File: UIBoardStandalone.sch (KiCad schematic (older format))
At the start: 45 parts, among them J10 Conn_02x15_Odd_Even, J17 Conn_02x08_Odd_Even, SW1 Button_P, SW10 Button_4, SW11 Button_8, SW12 Button_0, SW13 Button_2, SW14 Button_5, SW15 Button_3, SW16 Button_6, SW17 Button_9, SW18 Button_Z, SW2 Button_X, SW3 Button_S, SW4 Button_G, SW5 Button_R, SW6 Button_M, SW7 Button_7, SW8 Button_Y, SW9 Button_1, U1 HD1077R, U10 MM74C923, U11 HD1077R, U12 HD1077R, U13 HD1077R, U14 HD1077R, U15 HD1077R, U16 HD1077R, U17 HD1077R, U2 HD1077R, U3 HD1077R, U4 HD1077R, U5 HD1077R, U6 HD1077R, U7 HD1077R, U8 HD1077R, U9 HD1077R

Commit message: - Outline und erste Plazierungen
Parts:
- added H1, H2, H3, H4, H5, H6: MountingHole, MountingHole:MountingHole_3.2mm_M3_DIN965, symbol Mechanical:MountingHole
- SW1: renamed from SW2; footprint (none) -> Button_Switch_SMD:SW_SPST_EVQP0
- SW10: renamed from SW16; footprint (none) -> Button_Switch_SMD:SW_SPST_EVQP0
- SW11: renamed from SW3; footprint (none) -> Button_Switch_SMD:SW_SPST_EVQP0
- SW12: renamed from SW7; footprint (none) -> Button_Switch_SMD:SW_SPST_EVQP0
- SW13: renamed from SW11; footprint (none) -> Button_Switch_SMD:SW_SPST_EVQP0
- SW14: renamed from SW17; footprint (none) -> Button_Switch_SMD:SW_SPST_EVQP0
- SW15: renamed from SW4; footprint (none) -> Button_Switch_SMD:SW_SPST_EVQP0
- SW16: renamed from SW8; footprint (none) -> Button_Switch_SMD:SW_SPST_EVQP0
- SW17: renamed from SW12; footprint (none) -> Button_Switch_SMD:SW_SPST_EVQP0
- SW18: footprint (none) -> Button_Switch_SMD:SW_SPST_EVQP0
- SW2: renamed from SW5; footprint (none) -> Button_Switch_SMD:SW_SPST_EVQP0
- SW3: renamed from SW9; footprint (none) -> Button_Switch_SMD:SW_SPST_EVQP0
- SW4: renamed from SW13; footprint (none) -> Button_Switch_SMD:SW_SPST_EVQP0
- SW5: renamed from SW15; footprint (none) -> Button_Switch_SMD:SW_SPST_EVQP0
- SW6: renamed from SW1; footprint (none) -> Button_Switch_SMD:SW_SPST_EVQP0
- SW7: renamed from SW6; footprint (none) -> Button_Switch_SMD:SW_SPST_EVQP0
- SW8: renamed from SW10; footprint (none) -> Button_Switch_SMD:SW_SPST_EVQP0
- SW9: renamed from SW14; footprint (none) -> Button_Switch_SMD:SW_SPST_EVQP0
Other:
- moved on the sheet: SW12, SW13, SW16, SW17

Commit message: - Outline / Postionierung Zwischenstand
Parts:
- renumbered C85 to C2, C86 to C3, J17 to J1, J10 to J2, R61 to R1, U11 to U10, U12 to U11, U13 to U12, U14 to U13, U15 to U14, U16 to U15, U17 to U16, U10 to U17
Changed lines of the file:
@@
 $EndDescr
 $Comp
-L Connector_Generic:Conn_02x08_Odd_Even J17
+L Connector_Generic:Conn_02x08_Odd_Even J1
 U 1 1 5F670C41
 P 14100 4400
-AR Path="/5F670C41" Ref="J17"  Part="1"
+AR Path="/5F670C41" Ref="J1"  Part="1"
 AR Path="/602283F4/5F670C41" Ref="J?"  Part="1"
 AR Path="/6101166B/5F670C41" Ref="J17"  Part="1"
-F 0 "J17" H 14150 4917 50  0000 C CNN
+F 0 "J1" H 14150 4917 50  0000 C CNN
 F 1 "Conn_02x08_Odd_Even" H 14150 4826 50  0000 C CNN
 F 2 "Connector_PinHeader_2.54mm:PinHeader_2x08_P2.54mm_Vertical" H 14100 4400 50  0001 C CNN
@@
 ButtonA2GND
 $Comp
-L 74xx:MM74C923 U10
+L 74xx:MM74C923 U17
 U 1 1 60D1026E
 P 12800 7000
-F 0 "U10" H 12950 7800 50  0000 C CNN
+F 0 "U17" H 12950 7800 50  0000 C CNN
 F 1 "MM74C923" H 13100 7700 50  0000 C CNN
 F 2 "Package_SO:SOIC-20W_7.5x12.8mm_P1.27mm" H 12800 7000 50  0001 C CNN
@@
 	13750 7200 13300 7200
 $Comp
-L Device:C C86
+L Device:C C3
 U 1 1 60DD134B
 P 14000 7650
-F 0 "C86" H 14115 7696 50  0000 L CNN
+F 0 "C3" H 14115 7696 50  0000 L CNN
 F 1 "224nF" H 14115 7605 50  0000 L CNN
 F 2 "" H 14038 7500 50  0001 C CNN
@@
 	14000 7400 14000 7500
 $Comp
-L Device:C C85
+L Device:C C2
 U 1 1 60E085DC
 P 13450 7650
-F 0 "C85" H 13565 7696 50  0000 L CNN
+F 0 "C2" H 13565 7696 50  0000 L CNN
 F 1 "52uF" H 13565 7605 50  0000 L CNN
 F 2 "" H 13488 7500 50  0001 C CNN
@@
 	8350 5250 10150 5250
 $Comp
-L Device:R_PHOTO R61
+L Device:R_PHOTO R1
 U 1 1 5FC1430B
 P 10800 4700
-F 0 "R61" H 10870 4746 50  0000 L CNN
+F 0 "R1" H 10870 4746 50  0000 L CNN
 F 1 "LDR" H 10870 4655 50  0000 L CNN
 F 2 "OptoDevice:R_LDR_4.9x4.2mm_P2.54mm_Vertical" V 10850 4450 50  0001 L CNN
@@
 	5050 7600 5050 7850
 $Comp
-L Connector_Generic:Conn_02x15_Odd_Even J10
+L Connector_Generic:Conn_02x15_Odd_Even J2
 U 1 1 60B2D605
 P 5550 4550
-AR Path="/60B2D605" Ref="J10"  Part="1"
+AR Path="/60B2D605" Ref="J2"  Part="1"
 AR Path="/6101166B/60B2D605" Ref="J10"  Part="1"
-F 0 "J10" H 5600 5467 50  0000 C CNN
+F 0 "J2" H 5600 5467 50  0000 C CNN
 F 1 "Conn_02x15_Odd_Even" H 5600 5376 50  0000 C CNN
 F 2 "Connector_PinHeader_2.54mm:PinHeader_2x15_P2.54mm_Vertical" H 5550 4550 50  0001 C CNN
@@
 $EndComp
 $Comp
-L TeKaDe:HD1077R U11
+L TeKaDe:HD1077R U10
 U 1 1 61191E3C
 P 9800 800
-F 0 "U11" H 9750 700 50  0000 L CNN
+F 0 "U10" H 9750 700 50  0000 L CNN
 F 1 "HD1077R" H 9600 800 50  0000 L CNN
 F 2 "TeKaDe:7SegmentLED_HD1077R" H 9800 900 50  0001 C CNN
@@
 $EndComp
 $Comp
-L TeKaDe:HD1077R U12
+L TeKaDe:HD1077R U11
 U 1 1 6119245E
 P 10500 800
-F 0 "U12" H 10450 700 50  0000 L CNN
+F 0 "U11" H 10450 700 50  0000 L CNN
 F 1 "HD1077R" H 10300 800 50  0000 L CNN
 F 2 "TeKaDe:7SegmentLED_HD1077R" H 10500 900 50  0001 C CNN
@@
 $EndComp
 $Comp
-L TeKaDe:HD1077R U13
+L TeKaDe:HD1077R U12
 U 1 1 61192B19
 P 11250 800
-F 0 "U13" H 11200 700 50  0000 L CNN
+F 0 "U12" H 11200 700 50  0000 L CNN
 F 1 "HD1077R" H 11050 800 50  0000 L CNN
 F 2 "TeKaDe:7SegmentLED_HD1077R" H 11250 900 50  0001 C CNN
@@
 $EndComp
 $Comp
-L TeKaDe:HD1077R U14
+L TeKaDe:HD1077R U13
 U 1 1 61193991
 P 12000 800
-F 0 "U14" H 11950 700 50  0000 L CNN
+F 0 "U13" H 11950 700 50  0000 L CNN
 F 1 "HD1077R" H 11800 800 50  0000 L CNN
 F 2 "TeKaDe:7SegmentLED_HD1077R" H 12000 900 50  0001 C CNN
@@
 $EndComp
 $Comp
-L TeKaDe:HD1077R U15
+L TeKaDe:HD1077R U14
 U 1 1 61194425
 P 12750 800
-F 0 "U15" H 12700 700 50  0000 L CNN
+F 0 "U14" H 12700 700 50  0000 L CNN
 F 1 "HD1077R" H 12550 800 50  0000 L CNN
 F 2 "TeKaDe:7SegmentLED_HD1077R" H 12750 900 50  0001 C CNN
@@
 $EndComp
 $Comp
-L TeKaDe:HD1077R U16
+L TeKaDe:HD1077R U15
 U 1 1 611949C1
 P 13450 800
-F 0 "U16" H 13400 700 50  0000 L CNN
+F 0 "U15" H 13400 700 50  0000 L CNN
 F 1 "HD1077R" H 13250 800 50  0000 L CNN
 F 2 "TeKaDe:7SegmentLED_HD1077R" H 13450 900 50  0001 C CNN
@@
 $EndComp
 $Comp
-L TeKaDe:HD1077R U17
+L TeKaDe:HD1077R U16
 U 1 1 6119568C
 P 14200 800
-F 0 "U17" H 14150 700 50  0000 L CNN
+F 0 "U16" H 14150 700 50  0000 L CNN
 F 1 "HD1077R" H 14000 800 50  0000 L CNN
 F 2 "TeKaDe:7SegmentLED_HD1077R" H 14200 900 50  0001 C CNN

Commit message: - erster Stand für Abmessungen
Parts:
- D1: value LED_RED -> LED_RD
- D2: value LED_YELLOW -> LED_YL
- D3: value LED_GREEN -> LED_GN
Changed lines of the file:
@@
 P 9650 4650
 F 0 "D1" V 9597 4730 50  0000 L CNN
-F 1 "LED_RED" V 9688 4730 50  0000 L CNN
+F 1 "LED_RD" V 9688 4730 50  0000 L CNN
 F 2 "LED_THT:LED_D5.0mm" H 9650 4650 50  0001 C CNN
 F 3 "~" H 9650 4650 50  0001 C CNN
@@
 P 9150 4650
 F 0 "D2" V 9097 4730 50  0000 L CNN
-F 1 "LED_YELLOW" V 9188 4730 50  0000 L CNN
+F 1 "LED_YL" V 9188 4730 50  0000 L CNN
 F 2 "LED_THT:LED_D5.0mm" H 9150 4650 50  0001 C CNN
 F 3 "~" H 9150 4650 50  0001 C CNN
@@
 P 8500 4650
 F 0 "D3" V 8447 4730 50  0000 L CNN
-F 1 "LED_GREEN" V 8538 4730 50  0000 L CNN
+F 1 "LED_GN" V 8538 4730 50  0000 L CNN
 F 2 "LED_THT:LED_D5.0mm" H 8500 4650 50  0001 C CNN
 F 3 "~" H 8500 4650 50  0001 C CNN

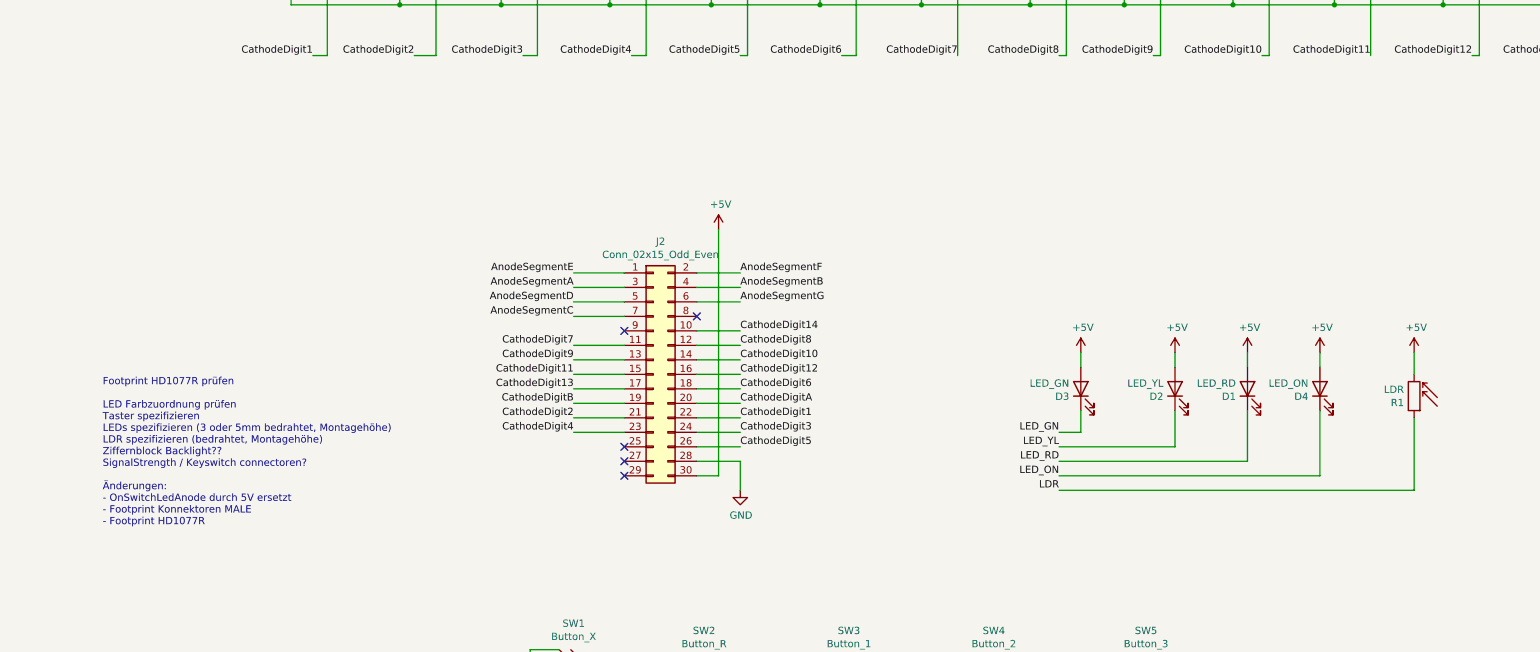
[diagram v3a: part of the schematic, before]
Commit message: [fix:] measurement errors [add:] backlight LEDs
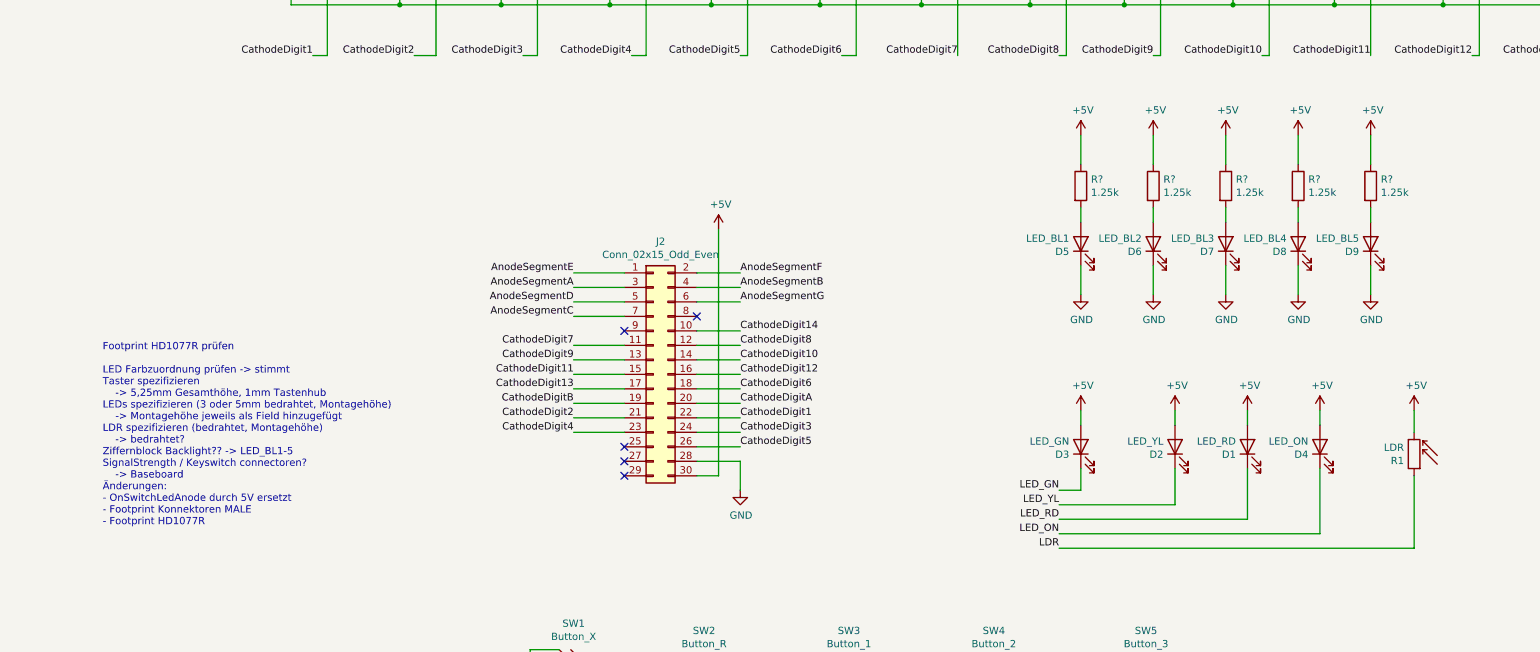
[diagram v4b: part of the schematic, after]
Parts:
- added D5: LED_BL1, LED_THT:LED_D3.0mm, symbol Device:LED
- added D6: LED_BL2, LED_THT:LED_D3.0mm, symbol Device:LED
- added D7: LED_BL3, LED_THT:LED_D3.0mm, symbol Device:LED
- added D8: LED_BL4, LED_THT:LED_D3.0mm, symbol Device:LED
- added D9: LED_BL5, LED_THT:LED_D3.0mm, symbol Device:LED
- added R? (x5): 1.25k, symbol Device:R
- D1, D2, D3: Montagehöhe (none) -> 9mm
- D4: Montagehöhe (none) -> 8mm
- R1: Montagehöhe (none) -> 7mm
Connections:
- net +5V: now also R?.1, R?.1, R?.1, R?.1, R?.1
- net GND: now also D5.1 (K), D6.1 (K), D7.1 (K), D8.1 (K), D9.1 (K)
- new net: D5.2 (A), R?.2
- new net: D6.2 (A), R?.2
- new net: D7.2 (A), R?.2
- new net: D8.2 (A), R?.2
- new net: D9.2 (A), R?.2
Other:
- note added: "Footprint HD1077R prüfen\n\nLED Farbzuordnung prüfen -> stimmt\nTaster spezifizieren\n -> 5,25mm Gesamthöhe, 1mm Tastenhub\nLEDs spezifizieren (3 oder 5mm bedrahtet, Montagehöhe)\n -> Montagehöhe jeweils als Field hinzugefügt\nLDR spezifizieren (bedrahtet, Montagehöhe)\n -> bedrahtet?\nZiffernblock Backlight?? -> LED_BL1-5\nSignalStrength / Keyswitch connectoren?\n -> Baseboard\nÄnderungen:\n- On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"
- note removed: "Footprint HD1077R prüfen\n\nLED Farbzuordnung prüfen\nTaster spezifizieren\nLEDs spezifizieren (3 oder 5mm bedrahtet, Montagehöhe)\nLDR spezifizieren (bedrahtet, Montagehöhe)\nZiffernblock Backlight??\nSignalStrength / Keyswitch connectoren?\n\nÄnderungen:\n- OnSwitchLedAnode durch 5V ersetzt\n- Footprint Konnektoren MALE\n- Footprint HD1077R"
- moved on the sheet: D1, D2, D3, D4, R1

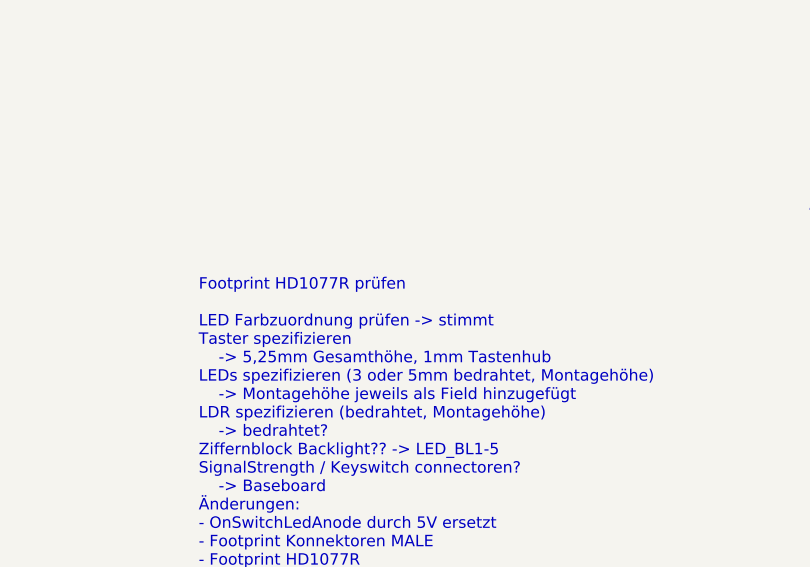
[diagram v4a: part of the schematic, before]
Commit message: [mod:] Note updates, KeySwitch mechanical definition
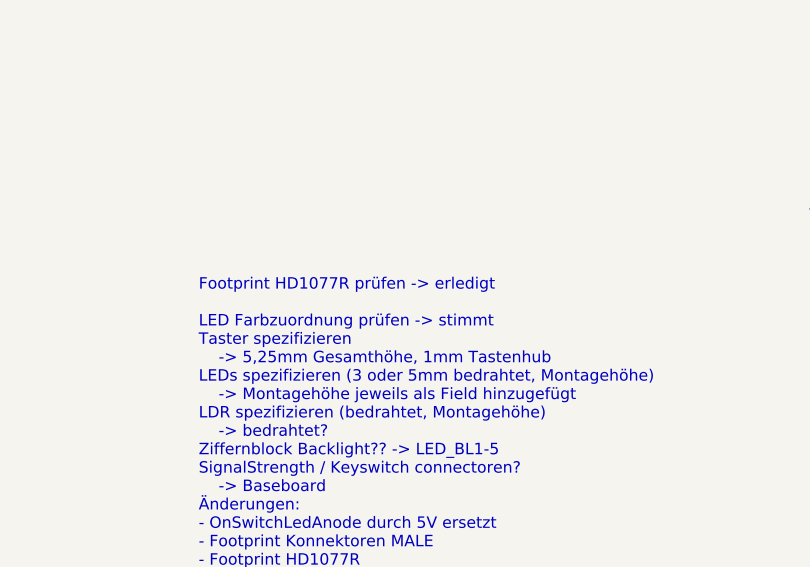
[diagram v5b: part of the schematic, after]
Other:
- note added: "Footprint HD1077R prüfen -> erledigt\n\nLED Farbzuordnung prüfen -> stimmt\nTaster spezifizieren\n -> 5,25mm Gesamthöhe, 1mm Tastenhub\nLEDs spezifizieren (3 oder 5mm bedrahtet, Montagehöhe)\n -> Montagehöhe jeweils als Field hinzugefügt\nLDR spezifizieren (bedrahtet, Montagehöhe)\n -> bedrahtet?\nZiffernblock Backlight?? -> LED_BL1-5\nSignalStrength / Keyswitch connectoren?\n -> Baseboard\nÄnder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"
- note removed: "Footprint HD1077R prüfen\n\nLED Farbzuordnung prüfen -> stimmt\nTaster spezifizieren\n -> 5,25mm Gesamthöhe, 1mm Tastenhub\nLEDs spezifizieren (3 oder 5mm bedrahtet, Montagehöhe)\n -> Montagehöhe jeweils als Field hinzugefügt\nLDR spezifizieren (bedrahtet, Montagehöhe)\n -> bedrahtet?\nZiffernblock Backlight?? -> LED_BL1-5\nSignalStrength / Keyswitch connectoren?\n -> Baseboard\nÄnderungen:\n- On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"
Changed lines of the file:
@@
 LED_GN
 Text Notes 1750 5600 0    50   ~ 0
-Footprint HD1077R prüfen\n\nLED Farbzuordnung prüfen -> stimmt\nTaster spezifizieren\n    -> 5,25mm Gesamthöhe, 1mm Tastenhub\nLEDs spezifizieren (3 oder 5mm bedrahtet, Montagehöhe)\n    -> Montagehöhe jeweils als Field hinzugefügt\nLDR spezifizieren (bedrahtet, Montagehöhe)\n    -> bedrahtet?\nZiffernblock Backlight?? -> LED_BL1-5\nSignalStrength / Keyswitch connectoren?\n    -> Baseboard\nÄnderungen:\n- OnSwitchLedAnode durch 5V ersetzt\n- Footprint Konnektoren MALE\n- Footprint HD1077R
+Footprint HD1077R prüfen -> erledigt\n\nLED Farbzuordnung prüfen -> stimmt\nTaster spezifizieren\n    -> 5,25mm Gesamthöhe, 1mm Tastenhub\nLEDs spezifizieren (3 oder 5mm bedrahtet, Montagehöhe)\n    -> Montagehöhe jeweils als Field hinzugefügt\nLDR spezifizieren (bedrahtet, Montagehöhe)\n    -> bedrahtet?\nZiffernblock Backlight?? -> LED_BL1-5\nSignalStrength / Keyswitch connectoren?\n    -> Baseboard\nÄnderungen:\n- OnSwitchLedAnode durch 5V ersetzt\n- Footprint Konnektoren MALE\n- Footprint HD1077R
 Wire Wire Line
 	12500 4700 12500 4600
